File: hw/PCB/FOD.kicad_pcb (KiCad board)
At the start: 2 copper layers, 48 x 95.6 mm, 29 parts, among them J1 USB_B_Micro, J2 Programmer, J3 SMA, U0 AP7215-33YG-13, U1 SAMD21G, U2 Payload, U3 SN754410, U4 RFM69HCW, Y1 32.768kHz

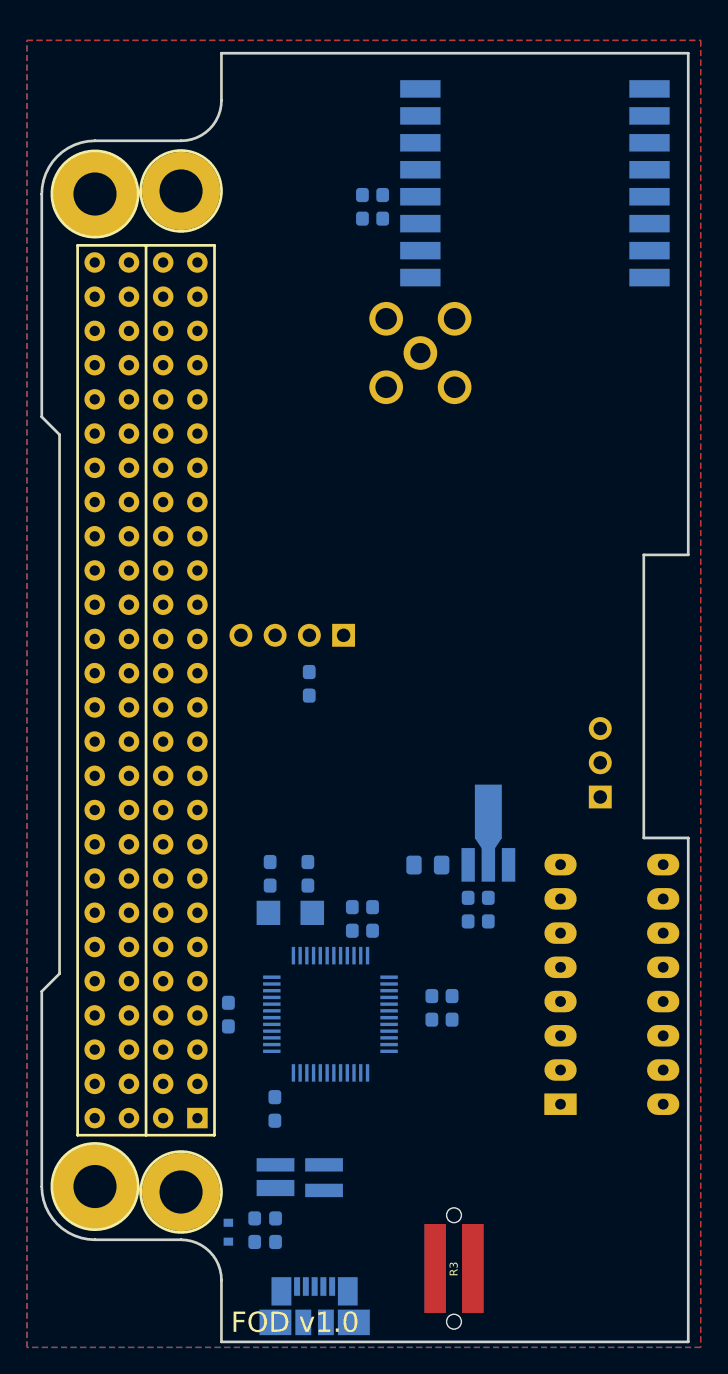
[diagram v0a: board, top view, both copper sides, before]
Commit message: Fixed some dimensions of the FOD's PCB.
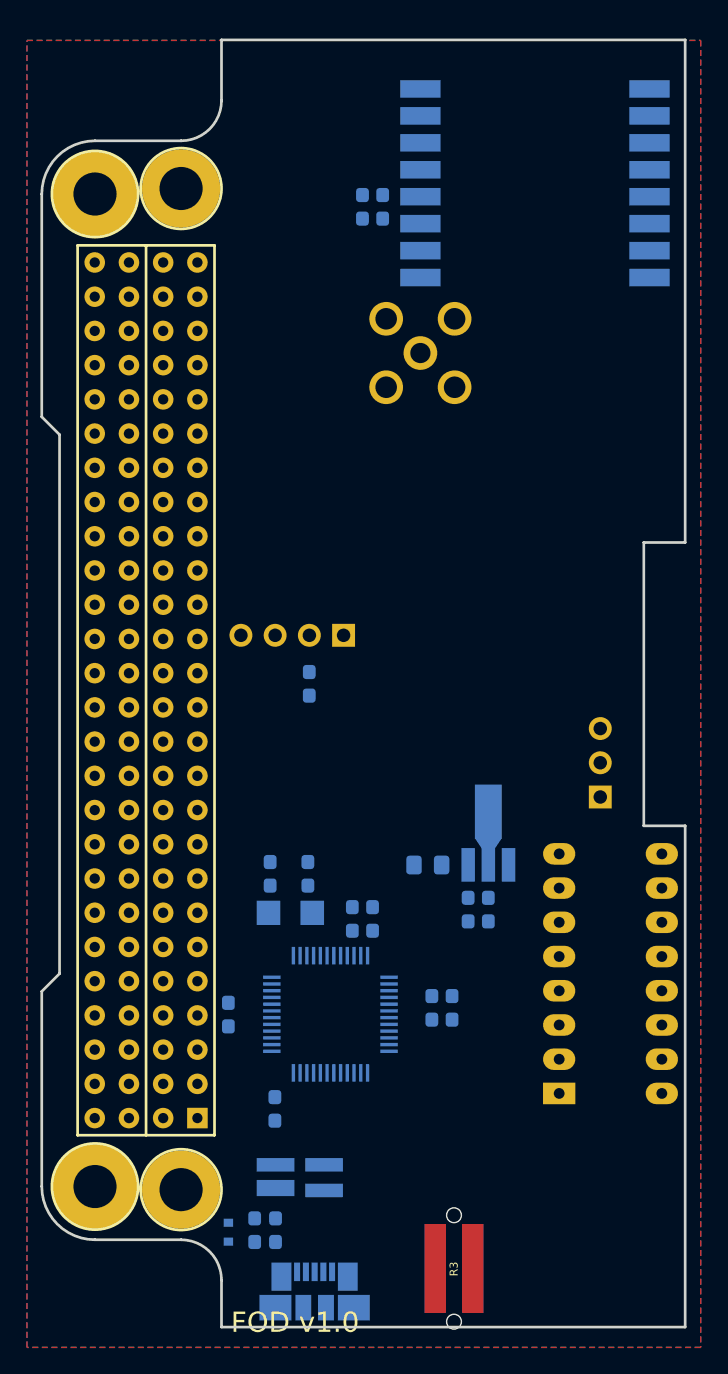
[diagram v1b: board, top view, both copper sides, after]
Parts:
- moved J1 1.09 mm to (139.3, 139.8)
- moved U3 0.81 mm to (157.5, 125.2)
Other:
- board size 48 x 95.6 mm -> 47.8 x 95.5 mm
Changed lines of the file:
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@@
       (effects (font (size 1 1) (thickness 0.15)))
     )
-    (fp_circle (center 6.388 -73.888) (end 9.388 -73.888) (layer F.SilkS) (width 0.2))
+    (fp_arc (start 6.39 6.95) (end 9.39 6.95) (angle -90) (layer Edge.Cuts) (width 0.2))
+    (fp_circle (center 6.39 -74.07) (end 9.39 -74.07) (layer F.SilkS) (width 0.2))
     (fp_circle (center 0 -73.66) (end 3.2 -73.66) (layer F.SilkS) (width 0.2))
-    (fp_circle (center 6.388 0.406) (end 9.388 0.406) (layer F.SilkS) (width 0.2))
+    (fp_circle (center 6.39 0.23) (end 9.39 0.23) (layer F.SilkS) (width 0.2))
     (fp_circle (center 0 0) (end 3.2 0) (layer F.SilkS) (width 0.2))
     (fp_line (start 3.79 -69.85) (end 3.79 -3.81) (layer F.SilkS) (width 0.2))
@@
     (fp_line (start -3.95 -14.48) (end -2.63 -15.8) (layer Edge.Cuts) (width 0.2))
     (fp_line (start -2.63 -15.8) (end -2.63 -55.8) (layer Edge.Cuts) (width 0.2))
-    (fp_line (start 9.388 6.95) (end 9.388 11.53) (layer Edge.Cuts) (width 0.2))
-    (fp_line (start 6.388 -77.61) (end 0 -77.61) (layer Edge.Cuts) (width 0.2))
-    (fp_arc (start 6.388 -80.61) (end 6.388 -77.61) (angle -90) (layer Edge.Cuts) (width 0.2))
-    (fp_line (start 9.388 -84.11) (end 9.388 -80.61) (layer Edge.Cuts) (width 0.2))
-    (fp_arc (start 6.388 6.95) (end 9.388 6.95) (angle -90) (layer Edge.Cuts) (width 0.2))
-    (fp_line (start 0 3.95) (end 6.388 3.95) (layer Edge.Cuts) (width 0.2))
+    (fp_line (start 9.39 6.95) (end 9.39 10.43) (layer Edge.Cuts) (width 0.2))
+    (fp_line (start 6.39 -77.61) (end 0 -77.61) (layer Edge.Cuts) (width 0.2))
+    (fp_arc (start 6.39 -80.61) (end 6.39 -77.61) (angle -90) (layer Edge.Cuts) (width 0.2))
+    (fp_line (start 9.39 -85.1) (end 9.39 -80.61) (layer Edge.Cuts) (width 0.2))
+    (fp_line (start 0 3.95) (end 6.39 3.95) (layer Edge.Cuts) (width 0.2))
     (fp_arc (start 0 0) (end -3.95 0) (angle -90) (layer Edge.Cuts) (width 0.2))
     (fp_arc (start 0 -73.66) (end 0 -77.61) (angle -90) (layer Edge.Cuts) (width 0.2))
     (fp_line (start -3.95 -14.48) (end -3.95 0) (layer Edge.Cuts) (width 0.2))
-    (fp_line (start 44.03 -84.11) (end 9.388 -84.11) (layer Edge.Cuts) (width 0.2))
-    (fp_line (start 44.03 -46.88) (end 44.03 -84.11) (layer Edge.Cuts) (width 0.2))
-    (fp_line (start 40.73 -46.88) (end 44.03 -46.88) (layer Edge.Cuts) (width 0.2))
-    (fp_line (start 40.73 -25.87) (end 40.73 -46.88) (layer Edge.Cuts) (width 0.2))
-    (fp_line (start 44.03 -25.87) (end 40.73 -25.87) (layer Edge.Cuts) (width 0.2))
-    (fp_line (start 44.03 11.53) (end 44.03 -25.87) (layer Edge.Cuts) (width 0.2))
-    (fp_line (start 9.388 11.53) (end 44.03 11.53) (layer Edge.Cuts) (width 0.2))
-    (pad "" np_thru_hole circle (at 6.388 0.406) (size 5.8 5.8) (drill 3.2) (layers *.Cu *.Mask))
-    (pad "" np_thru_hole circle (at 6.388 -73.888) (size 5.8 5.8) (drill 3.2) (layers *.Cu *.Mask))
+    (fp_line (start 43.8 -85.1) (end 9.39 -85.1) (layer Edge.Cuts) (width 0.2))
+    (fp_line (start 43.8 -47.8) (end 43.8 -85.1) (layer Edge.Cuts) (width 0.2))
+    (fp_line (start 40.73 -47.8) (end 43.8 -47.8) (layer Edge.Cuts) (width 0.2))
+    (fp_line (start 40.73 -26.77) (end 40.73 -47.8) (layer Edge.Cuts) (width 0.2))
+    (fp_line (start 43.8 -26.77) (end 40.73 -26.77) (layer Edge.Cuts) (width 0.2))
+    (fp_line (start 43.8 -26.77) (end 43.8 10.43) (layer Edge.Cuts) (width 0.2))
+    (fp_line (start 9.39 10.43) (end 43.8 10.43) (layer Edge.Cuts) (width 0.2))
+    (pad "" np_thru_hole circle (at 6.39 0.23) (size 5.8 5.8) (drill 3.2) (layers *.Cu *.Mask))
+    (pad "" np_thru_hole circle (at 6.39 -74.07) (size 5.8 5.8) (drill 3.2) (layers *.Cu *.Mask))
     (pad 53 thru_hole circle (at 2.52 -5.08) (size 1.524 1.524) (drill 0.762) (layers *.Cu *.Mask)
       (net 152 "Net-(U2-Pad53)"))
@@
   )
   (module Connector_USB:USB_Micro-B_Molex_47346-0001 (layer B.Cu)
-    (at 139.349998 140.94 180)
+    (at 139.349998 139.85 180)
     (descr "Micro USB B receptable with flange, bottom-mount, SMD, right-angle (http://www.molex.com/pdm_docs/sd/473460001_sd.pdf)")
     (tags "Micro B USB SMD")
@@
   )
   (module Package_DIP:DIP-16_W7.62mm_LongPads (layer B.Cu)
-    (at 157.6 125.95)
+    (at 157.5 125.15)
     (descr "16-lead though-hole mounted DIP package, row spacing 7.62 mm (300 mils), LongPads")
     (tags "THT DIP DIL PDIP 2.54mm 7.62mm 300mil LongPads")

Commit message: Added switch to detect the deplyment status. Routed all connections.
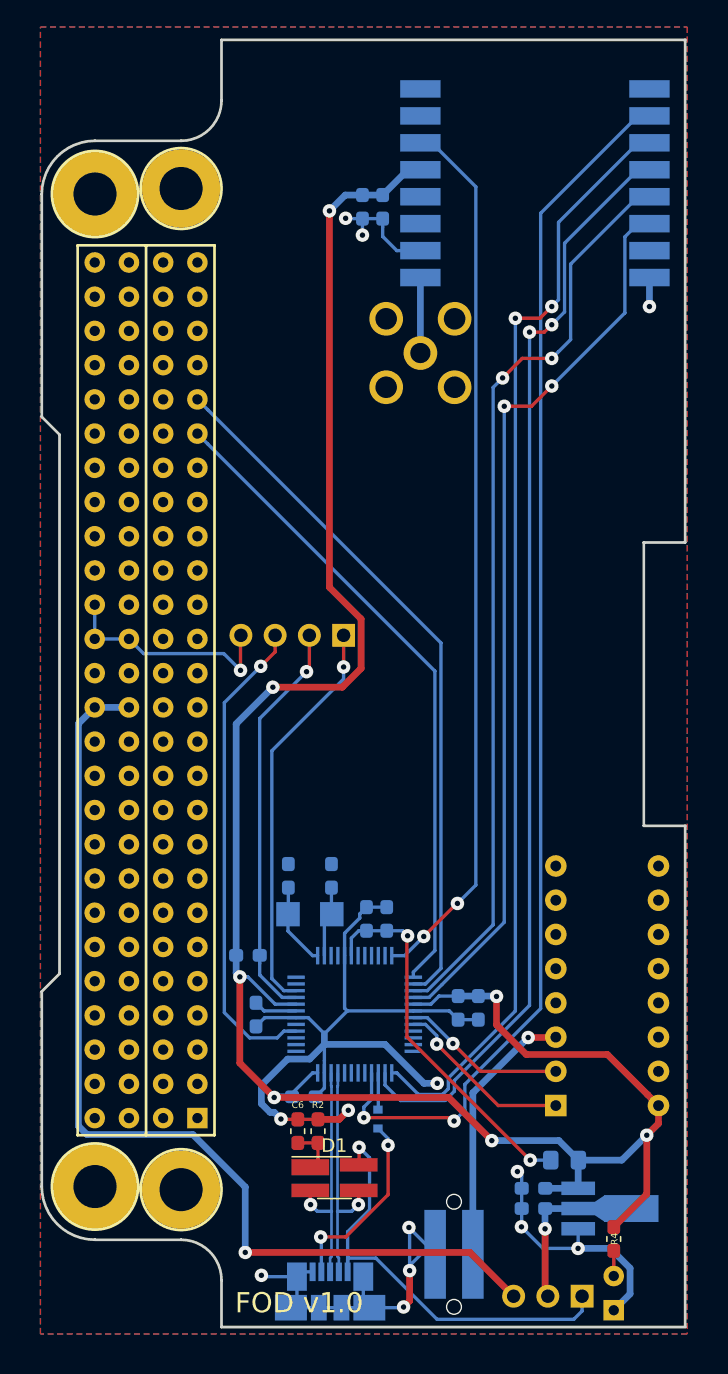
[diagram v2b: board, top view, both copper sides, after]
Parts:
- added R4: 1K, Resistor_SMD:R_0603_1608Metric_Pad1.05x0.95mm_HandSolder, F.Cu at (161.6, 135.9)
- added U5: AV4524_2PIN, Interrupt:AV4524_2PIN, B.Cu at (161.6, 138.7)
- C6, D1, R2: moved to F.Cu
- R3: moved to B.Cu
- U3: footprint Package_DIP:DIP-16_W7.62mm_LongPads -> Package_DIP:DIP-16_W7.62mm
- moved JP1 37.1 mm to (159.2, 140.2), turned to 90 degrees
- moved U0 28.8 mm to (160.9, 133.7), turned to 0 degrees
- moved L1 24.1 mm to (157.9, 130.1)
- moved Cr1 22.4 mm to (155.6, 133.7), turned to 180 degrees
- moved Cr2 21.2 mm to (155.6, 132.2), turned to 180 degrees
- moved R1 20.7 mm to (134.4, 114.9), turned to 0 degrees
- moved D3 13.9 mm to (144.1, 127.0)
- moved C6 8.02 mm to (138.1, 128.0), turned to 90 degrees
- moved R2 8.00 mm to (139.6, 128.0), turned to 90 degrees
- moved D1 2.57 mm to (140.8, 131.4)
- moved C3b1 2.33 mm to (138.6, 125.4), turned to 0 degrees
- moved C5 2.05 mm to (135.0, 119.3)
- moved C3a1 1.95 mm to (150.0, 118.8)
- moved C4 1.95 mm to (151.5, 118.8)
- moved U1 1.80 mm to (142.3, 119.3)
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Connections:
- U1 pad 12: /A6 -> /TRX_INT
- U1 pad 15: /PIN_2 -> /TRX_NSS
- U1 pad 16: /PIN_3 -> /TRX_RST
- U1 pad 19: /PIN_4 -> /DPL_SIG
- U1 pad 20: /DPL_SIG -> /DPL_EN
- U3 pad 16: /5V0 -> /3V3
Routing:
- net /3V3: track 0.00 -> 160.4 mm, vias 0 -> 7
- net GND: track 0.00 -> 133.1 mm, vias 0 -> 14
- net /MISO: track 0.00 -> 91.5 mm, vias 0 -> 2
- net /MOSI: track 0.00 -> 83.0 mm, vias 0 -> 2
- net /SCK: track 0.00 -> 82.3 mm, vias 0 -> 2
- net /VIN: track 0.00 -> 74.5 mm, vias 0 -> 1
- net /TRX_NSS: track 0.00 -> 68.6 mm, vias 0 -> 2
- net /TRX_RST: track 0.00 -> 67.1 mm, vias 0 -> 2
- net /TRX_INT: track 0.00 -> 65.7 mm, vias 0 -> 2
- net /SCL: track 0.00 -> 52.2 mm
- net /SDA: track 0.00 -> 48.3 mm
- net /RESET: track 0.00 -> 35.9 mm, vias 0 -> 1
- net /VBUS: track 0.00 -> 33.2 mm, vias 0 -> 1
- net /SWCLK: track 0.00 -> 30.1 mm, vias 0 -> 1
- net /SWDIO: track 0.00 -> 29.9 mm, vias 0 -> 1
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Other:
- net class Default: via_dia 0.8 -> 1
- net class Power added: clearance 0.2, trace_width 0.5, via_dia 1, via_drill 0.4
- net class uC: via_drill 0.7 -> 0.4

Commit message: Made space for the interrupter.
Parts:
- moved R4 1.69 mm to (159.9, 135.9)
- moved U5 1.69 mm to (159.9, 138.7)
- moved JP1 1.69 mm to (157.5, 140.2)
- moved R3 1.69 mm to (148.0, 137.1)
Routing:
- net GND: track 133.1 -> 128.9 mm, vias 14 -> 13
- net /3V3: track 160.4 -> 156.9 mm
- net /VBUS: track 33.2 -> 31.6 mm, vias 1 -> 4
- net /VIN: track 74.5 -> 73.8 mm
- net /Deploy/DPL_OUT: track 19.9 -> 20.5 mm
- net /5V0: track 13.0 -> 13.5 mm

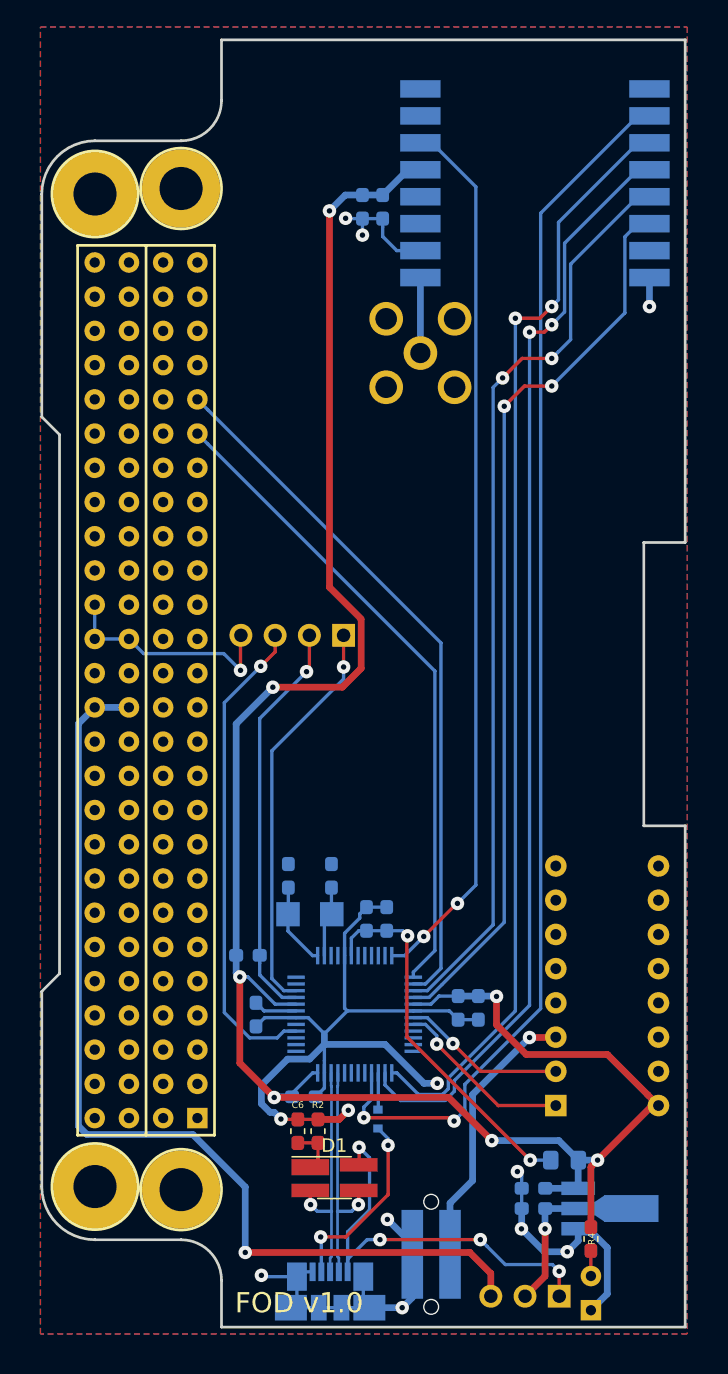
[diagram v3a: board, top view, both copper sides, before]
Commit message: Fixed space conflict between the interrupter and the voltage regulator.
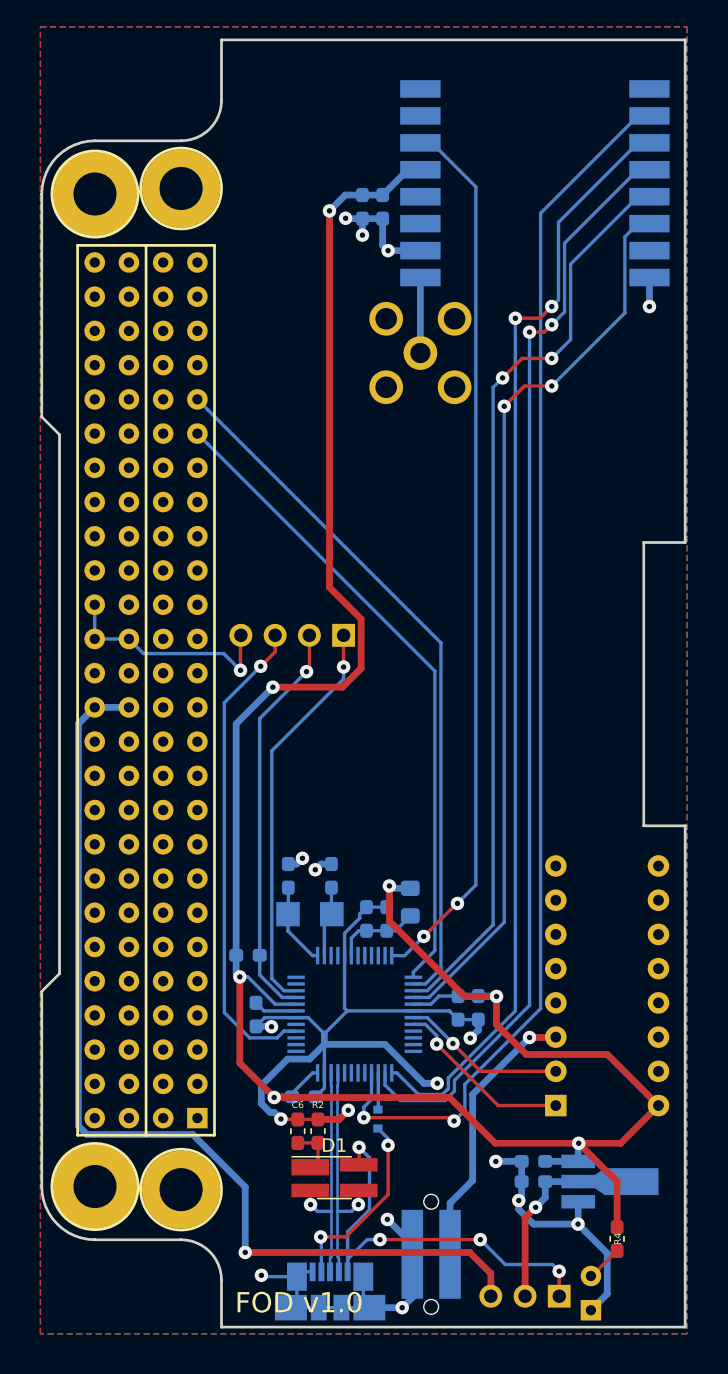
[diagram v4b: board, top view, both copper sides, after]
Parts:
- moved L1 22.3 mm to (146.4, 111.0), turned to 90 degrees
- moved Cr1 2.00 mm to (155.6, 131.7)
- moved Cr2 2.00 mm to (155.6, 130.2)
- moved U0 2.00 mm to (160.9, 131.7)
- moved R4 1.94 mm to (161.8, 135.9)
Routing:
- net /VDDANA: track 27.8 -> 6.36 mm, vias 2 -> 0
- net /3V3: track 156.9 -> 171.9 mm
- net GND: track 128.9 -> 136.1 mm, vias 13 -> 18
- net /5V0: track 13.5 -> 15.5 mm
- net /Deploy/DPL_STA: track 1.88 -> 2.72 mm
